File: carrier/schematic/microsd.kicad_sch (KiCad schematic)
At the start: 14 parts, among them J12001 TF-01A, U12001 TXS02612RTWR, U12002 TPD6E001RSER

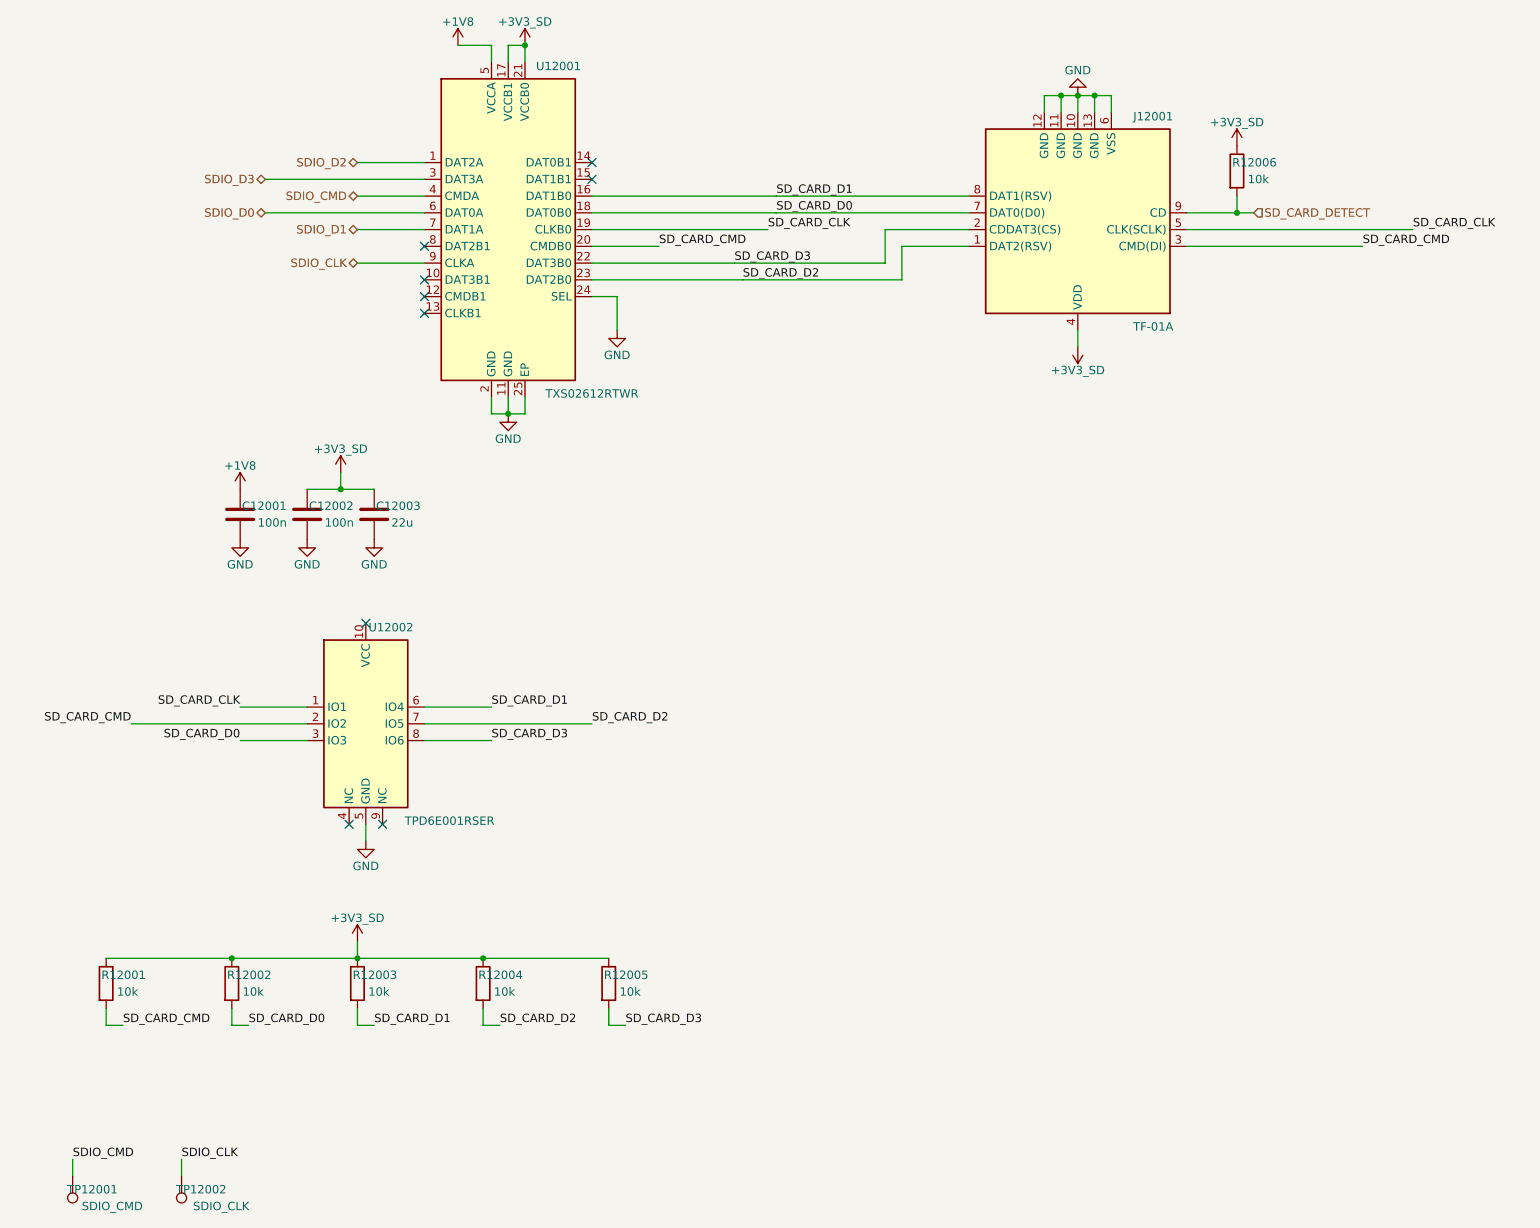
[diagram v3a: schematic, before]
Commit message: carrier: consolidated regen for round-6 audit fixes + PLAN RESOLVED
schgen board regen after SD-1 / HDMIRX-1 / HDMIRX-2 / LCD-1: 23 sheets, all
gates green (board-link, ERC=0, power-tree 16 regs/0 findings, testpoints,
SPICE 21 checks, visual). Goldens drift only on the 3 touched sheets
(microsd/hdmi_rx/lcd schematic+render), BOM (microsd:C4 100n, hdmi_rx:R5 10k,
lcd:C2 2.2u/C125847), reports, floorplan. PLAN findings marked RESOLVED
(HDMIRX-1 = documented verified-part DNP). selftest 44/44 + byte-deterministic.

Co-Authored-By: Claude Fable 5 <noreply@anthropic.com>
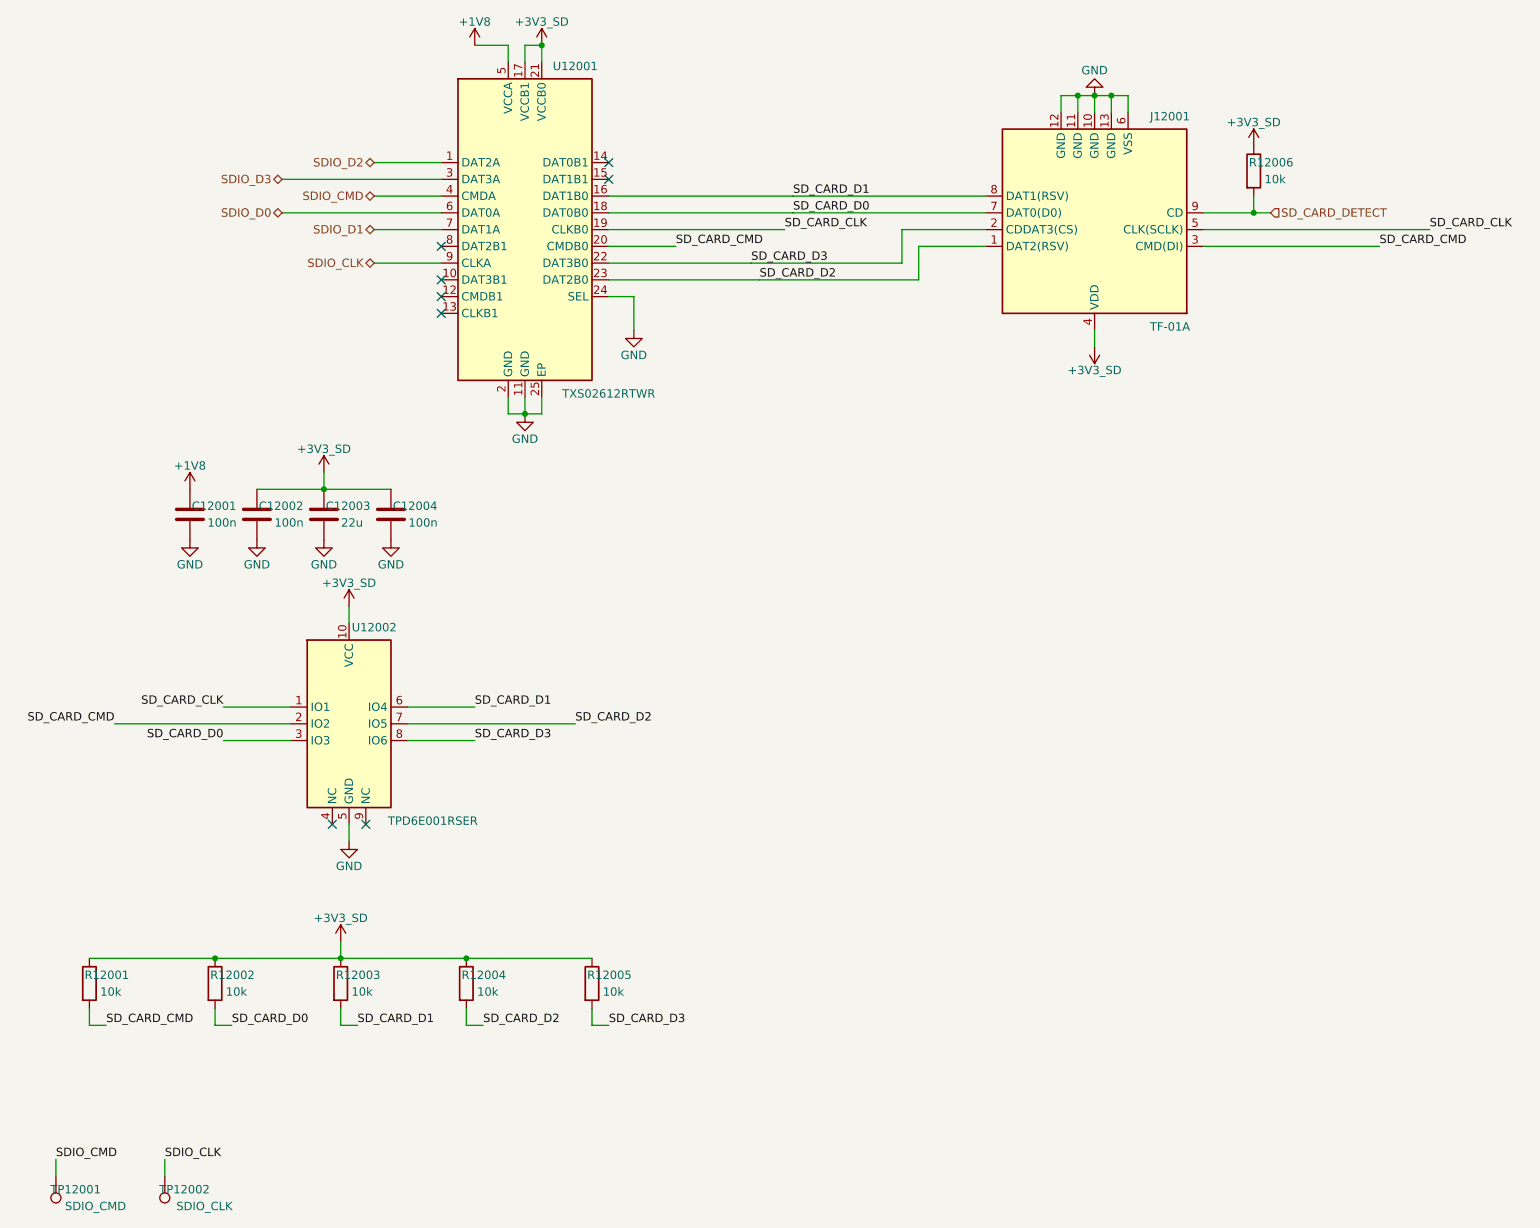
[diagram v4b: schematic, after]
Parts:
- added TP12002: SDIO_CLK, TestPoint:TestPoint_Pad_D1.5mm, symbol Connector:TestPoint
- C12004: renamed from U12002; value TPD6E001RSER -> 100n; footprint TPD6E001RSER:TPD6E001RSER -> (none); symbol TPD6E001RSER:TPD6E001RSER -> Device:C; LCSC C1973318 -> C14663
- R12005: renamed from TP12001; value SDIO_CMD -> 10k; footprint TestPoint:TestPoint_Pad_D1.5mm -> Resistor_SMD:R_0603_1608Metric; symbol Connector:TestPoint -> Device:R; BOM exclude -> (none); LCSC (none) -> C25804
- TP12001: renamed from TP12002; value SDIO_CLK -> SDIO_CMD
- U12002: renamed from R12001; value 10k -> TPD6E001RSER; footprint Resistor_SMD:R_0603_1608Metric -> TPD6E001RSER:TPD6E001RSER; symbol Device:R -> TPD6E001RSER:TPD6E001RSER; LCSC C25804 -> C1973318
- renumbered R12002 to R12001, R12003 to R12002, R12004 to R12003, R12005 to R12004
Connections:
- net +3V3_SD: now also C12004.1, R12005.1, U12002.10 (VCC); no longer U12002.1
- net GND: now also C12004.2, U12002.5 (GND); no longer C12004.5 (GND)
- net SDIO_CLK: now also TP12002.1; no longer TP12001.1
- net SDIO_CMD: now also TP12001.1; no longer R12005.1
- net SD_CARD_CLK: now also U12002.1 (IO1); no longer C12004.1 (IO1)
- net SD_CARD_CMD: now also R12001.2; no longer C12004.2 (IO2)
- net SD_CARD_D0: now also R12002.2, U12002.3 (IO3); no longer C12004.3 (IO3), R12001.2
- net SD_CARD_D1: now also R12003.2, U12002.6 (IO4); no longer C12004.6 (IO4), R12002.2
- net SD_CARD_D2: now also R12004.2, U12002.7 (IO5); no longer C12004.7 (IO5), R12003.2
- net SD_CARD_D3: now also R12005.2, U12002.8 (IO6); no longer C12004.8 (IO6), R12004.2
- no-connect marks 9 -> 8
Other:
- moved on the sheet: C12001, C12002, C12003, J12001, R12001, R12002, R12003, R12004, R12006, TP12001, U12001

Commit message: DEF-3: default footprints for inline passives + BOM footprint gate
16 inline Device:C/Device:R passives (decouple()/part() calls in microsd,
uart_bridge, usb_pd, usbc_otg) carried footprint='' — so the JLC BOM had 6
line items an assembler literally cannot place. model.part() now defaults a
standard SMD footprint when none is given: Device:R -> 0603, Device:C -> 0603
(or 0805 for >= 1 uF bulk), matching every inline passive's JLC Basic package
(100n/200p 0603, 10u/22u 0805, 1k/22k1/47k5 0603). use_part is unaffected (it
always supplies the library footprint). A new BOM FOOTPRINT GATE in cmd_board
fails the board if any BOM line is still footprint-less, backstopping the
non-passive case. board PASS, all 81 BOM lines placeable, 25 goldens match
(footprint is a hidden field — renders unchanged), selftest 44/44, m1 PASS.
The floorplan now gives those passives real courtyards.

Co-Authored-By: Claude Opus 4.8 <noreply@anthropic.com>
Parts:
- C12001, C12004: footprint (none) -> Capacitor_SMD:C_0603_1608Metric
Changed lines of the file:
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@@
 		(property
 			"Footprint"
-			""
+			"Capacitor_SMD:C_0603_1608Metric"
 			(at 123.19 133.35 0)
 			(effects
@@
 		(property
 			"Footprint"
-			""
+			"Capacitor_SMD:C_0603_1608Metric"
 			(at 153.67 133.35 0)
 			(effects

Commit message: DEF-6: netlist the HDMI-RX TMDS sink termination (new hdmi_rx_term sheet)
The HDMI-RX sink REQUIRES 8x 49.9 ohm/pair-to-AVCC source termination (a
7-series HR bank does not self-terminate TMDS_33) — without it HDMI RX simply
does not work. It had been carried for rounds as a docstring-only MANDATORY
layout note because the resistors belong at the FPGA-bank (receiver) end and
the connector-sheet placer could not anchor an off-sheet AVCC trunk. DEF-6
promotes it to a real, netlisted, gate-checked, BOM-counted network on its own
sheet hdmi_rx_term.py: 8x 49.9R (C114625) from HDMI_RX_{D2,D1,D0,CLK}_{P,N} to
AVCC = +3V3 (bank-33 VCCO IS +3V3, the correct TMDS_33 termination voltage).

LINK PASS (the 3-way TMDS merge with hdmi_rx + som_j2), powertree accepts the
~64 mA termination load, render clean (LAW 1), board PASS 26 sheets,
deterministic, selftest 44/44, m1 PASS.

The 100n/1u AVCC bypass is a documented layout note (not netlisted): the
placer has no pattern for a rail-to-rail cap with no host part on an IC-less
sheet (a tracked placer-robustness follow-up). Inserting the sheet
alphabetically re-stamps the per-sheet reference uniquification of the 15
downstream sheets (U11001->U12001 etc.) — deterministic, a known consequence
of the position-based hierarchy numbering.

Co-Authored-By: Claude Opus 4.8 <noreply@anthropic.com>
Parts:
- renumbered C12001 to C13001, C12002 to C13002, C12003 to C13003, C12004 to C13004, J12001 to J13001, R12001 to R13001, R12002 to R13002, R12003 to R13003, R12004 to R13004, R12005 to R13005, R12006 to R13006, TP12001 to TP13001, TP12002 to TP13002, U12001 to U13001, U12002 to U13002
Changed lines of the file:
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@@
 		(property
 			"Reference"
-			"U12001"
+			"U13001"
 			(at 181.61 65.405 0)
 			(effects
@@
 				(path
 					"/c2797150-7a6e-556a-82f5-fdda13c31368/d897b633-e4e1-5c36-ba27-9e08872325fa"
-					(reference "U12001")
+					(reference "U13001")
 					(unit 1)
 				)
@@
 		(property
 			"Reference"
-			"J12001"
+			"J13001"
 			(at 271.78 73.025 0)
 			(effects
@@
 				(path
 					"/c2797150-7a6e-556a-82f5-fdda13c31368/d897b633-e4e1-5c36-ba27-9e08872325fa"
-					(reference "J12001")
+					(reference "J13001")
 					(unit 1)
 				)
@@
 		(property
 			"Reference"
-			"R12006"
+			"R13006"
 			(at 287.123 80.01 0)
 			(effects
@@
 				(path
 					"/c2797150-7a6e-556a-82f5-fdda13c31368/d897b633-e4e1-5c36-ba27-9e08872325fa"
-					(reference "R12006")
+					(reference "R13006")
 					(unit 1)
 				)
@@
 		(property
 			"Reference"
-			"C12001"
+			"C13001"
 			(at 126.849 132.08 0)
 			(effects
@@
 				(path
 					"/c2797150-7a6e-556a-82f5-fdda13c31368/d897b633-e4e1-5c36-ba27-9e08872325fa"
-					(reference "C12001")
+					(reference "C13001")
 					(unit 1)
 				)
@@
 		(property
 			"Reference"
-			"C12002"
+			"C13002"
 			(at 137.009 132.08 0)
 			(effects
@@
 				(path
 					"/c2797150-7a6e-556a-82f5-fdda13c31368/d897b633-e4e1-5c36-ba27-9e08872325fa"
-					(reference "C12002")
+					(reference "C13002")
 					(unit 1)
 				)
@@
 		(property
 			"Reference"
-			"C12003"
+			"C13003"
 			(at 147.169 132.08 0)
 			(effects
@@
 				(path
 					"/c2797150-7a6e-556a-82f5-fdda13c31368/d897b633-e4e1-5c36-ba27-9e08872325fa"
-					(reference "C12003")
+					(reference "C13003")
 					(unit 1)
 				)
@@
 		(property
 			"Reference"
-			"C12004"
+			"C13004"
 			(at 157.329 132.08 0)
 			(effects
@@
 				(path
 					"/c2797150-7a6e-556a-82f5-fdda13c31368/d897b633-e4e1-5c36-ba27-9e08872325fa"
-					(reference "C12004")
+					(reference "C13004")
 					(unit 1)
 				)
@@
 		(property
 			"Reference"
-			"U12002"
+			"U13002"
 			(at 151.13 150.495 0)
 			(effects
@@
 				(path
 					"/c2797150-7a6e-556a-82f5-fdda13c31368/d897b633-e4e1-5c36-ba27-9e08872325fa"
-					(reference "U12002")
+					(reference "U13002")
 					(unit 1)
 				)
@@
 		(property
 			"Reference"
-			"R12001"
+			"R13001"
 			(at 110.593 203.2 0)
 			(effects
@@
 				(path
 					"/c2797150-7a6e-556a-82f5-fdda13c31368/d897b633-e4e1-5c36-ba27-9e08872325fa"
-					(reference "R12001")
+					(reference "R13001")
 					(unit 1)
 				)
@@
 		(property
 			"Reference"
-			"R12002"
+			"R13002"
 			(at 129.643 203.2 0)
 			(effects
@@
 				(path
 					"/c2797150-7a6e-556a-82f5-fdda13c31368/d897b633-e4e1-5c36-ba27-9e08872325fa"
-					(reference "R12002")
+					(reference "R13002")
 					(unit 1)
 				)
@@
 		(property
 			"Reference"
-			"R12003"
+			"R13003"
 			(at 148.693 203.2 0)
 			(effects
@@
 				(path
 					"/c2797150-7a6e-556a-82f5-fdda13c31368/d897b633-e4e1-5c36-ba27-9e08872325fa"
-					(reference "R12003")
+					(reference "R13003")
 					(unit 1)
 				)
@@
 		(property
 			"Reference"
-			"R12004"
+			"R13004"
 			(at 167.743 203.2 0)
 			(effects
@@
 				(path
 					"/c2797150-7a6e-556a-82f5-fdda13c31368/d897b633-e4e1-5c36-ba27-9e08872325fa"
-					(reference "R12004")
+					(reference "R13004")
 					(unit 1)
 				)
@@
 		(property
 			"Reference"
-			"R12005"
+			"R13005"
 			(at 186.792 203.2 0)
 			(effects
@@
 				(path
 					"/c2797150-7a6e-556a-82f5-fdda13c31368/d897b633-e4e1-5c36-ba27-9e08872325fa"
-					(reference "R12005")
+					(reference "R13005")
 					(unit 1)
 				)
@@
 		(property
 			"Reference"
-			"TP12001"
+			"TP13001"
 			(at 105.862 235.712 0)
 			(effects
@@
 				(path
 					"/c2797150-7a6e-556a-82f5-fdda13c31368/d897b633-e4e1-5c36-ba27-9e08872325fa"
-					(reference "TP12001")
+					(reference "TP13001")
 					(unit 1)
 				)
@@
 		(property
 			"Reference"
-			"TP12002"
+			"TP13002"
 			(at 122.372 235.712 0)
 			(effects
@@
 				(path
 					"/c2797150-7a6e-556a-82f5-fdda13c31368/d897b633-e4e1-5c36-ba27-9e08872325fa"
-					(reference "TP12002")
+					(reference "TP13002")
 					(unit 1)
 				)
@@
 		(property
 			"Reference"
-			"#PWR12001"
+			"#PWR13001"
 			(at 190.5 102.87 0)
 			(effects
@@
 				(path
 					"/c2797150-7a6e-556a-82f5-fdda13c31368/d897b633-e4e1-5c36-ba27-9e08872325fa"
-					(reference "#PWR12001")
+					(reference "#PWR13001")
 					(unit 1)
 				)
@@
 		(property
 			"Reference"
-			"#PWR12002"
+			"#PWR13002"
 			(at 176.53 59.69 0)
 			(effects
@@
 				(path
 					"/c2797150-7a6e-556a-82f5-fdda13c31368/d897b633-e4e1-5c36-ba27-9e08872325fa"
-					(reference "#PWR12002")
+					(reference "#PWR13002")
 					(unit 1)
 				)
@@
 		(property
 			"Reference"
-			"#PWR12003"
+			"#PWR13003"
 			(at 166.37 59.69 0)
 			(effects
@@
 				(path
 					"/c2797150-7a6e-556a-82f5-fdda13c31368/d897b633-e4e1-5c36-ba27-9e08872325fa"
-					(reference "#PWR12003")
+					(reference "#PWR13003")
 					(unit 1)
 				)
@@
 		(property
 			"Reference"
-			"#PWR12004"
+			"#PWR13004"
 			(at 173.99 115.57 0)
 			(effects
@@
 				(path
 					"/c2797150-7a6e-556a-82f5-fdda13c31368/d897b633-e4e1-5c36-ba27-9e08872325fa"
-					(reference "#PWR12004")
+					(reference "#PWR13004")
 					(unit 1)
 				)
@@
 		(property
 			"Reference"
-			"#PWR12005"
+			"#PWR13005"
 			(at 284.48 74.93 0)
 			(effects
@@
 				(path
 					"/c2797150-7a6e-556a-82f5-fdda13c31368/d897b633-e4e1-5c36-ba27-9e08872325fa"
-					(reference "#PWR12005")
+					(reference "#PWR13005")
 					(unit 1)
 				)
@@
 		(property
 			"Reference"
-			"#PWR12006"
+			"#PWR13006"
 			(at 260.35 67.31 0)
 			(effects
@@
 				(path
 					"/c2797150-7a6e-556a-82f5-fdda13c31368/d897b633-e4e1-5c36-ba27-9e08872325fa"
-					(reference "#PWR12006")
+					(reference "#PWR13006")
 					(unit 1)
 				)
@@
 		(property
 			"Reference"
-			"#PWR12007"
+			"#PWR13007"
 			(at 260.35 105.41 0)
 			(effects
@@
 				(path
 					"/c2797150-7a6e-556a-82f5-fdda13c31368/d897b633-e4e1-5c36-ba27-9e08872325fa"
-					(reference "#PWR12007")
+					(reference "#PWR13007")
 					(unit 1)
 				)
@@
 		(property
 			"Reference"
-			"#PWR12008"
+			"#PWR13008"
 			(at 123.19 134.62 0)
 			(effects
@@
 				(path
 					"/c2797150-7a6e-556a-82f5-fdda13c31368/d897b633-e4e1-5c36-ba27-9e08872325fa"
-					(reference "#PWR12008")
+					(reference "#PWR13008")
 					(unit 1)
 				)
@@
 		(property
 			"Reference"
-			"#PWR12009"
+			"#PWR13009"
 			(at 123.19 127 0)
 			(effects
@@
 				(path
 					"/c2797150-7a6e-556a-82f5-fdda13c31368/d897b633-e4e1-5c36-ba27-9e08872325fa"
-					(reference "#PWR12009")
+					(reference "#PWR13009")
 					(unit 1)
 				)
@@
 		(property
 			"Reference"
-			"#PWR12010"
+			"#PWR13010"
 			(at 133.35 134.62 0)
 			(effects
@@
 				(path
 					"/c2797150-7a6e-556a-82f5-fdda13c31368/d897b633-e4e1-5c36-ba27-9e08872325fa"
-					(reference "#PWR12010")
+					(reference "#PWR13010")
 					(unit 1)
 				)
@@
 		(property
 			"Reference"
-			"#PWR12011"
+			"#PWR13011"
 			(at 143.51 134.62 0)
 			(effects
@@
 				(path
 					"/c2797150-7a6e-556a-82f5-fdda13c31368/d897b633-e4e1-5c36-ba27-9e08872325fa"
-					(reference "#PWR12011")
+					(reference "#PWR13011")
 					(unit 1)
 				)
@@
 		(property
 			"Reference"
-			"#PWR12012"
+			"#PWR13012"
 			(at 153.67 134.62 0)
 			(effects
@@
 				(path
 					"/c2797150-7a6e-556a-82f5-fdda13c31368/d897b633-e4e1-5c36-ba27-9e08872325fa"
-					(reference "#PWR12012")
+					(reference "#PWR13012")
 					(unit 1)
 				)
@@
 		(property
 			"Reference"
-			"#PWR12013"
+			"#PWR13013"
 			(at 143.51 124.46 0)
 			(effects
@@
 				(path
 					"/c2797150-7a6e-556a-82f5-fdda13c31368/d897b633-e4e1-5c36-ba27-9e08872325fa"
-					(reference "#PWR12013")
+					(reference "#PWR13013")
 					(unit 1)
 				)
@@
 		(property
 			"Reference"
-			"#PWR12014"
+			"#PWR13014"
 			(at 147.32 144.78 0)
 			(effects
@@
 				(path
 					"/c2797150-7a6e-556a-82f5-fdda13c31368/d897b633-e4e1-5c36-ba27-9e08872325fa"
-					(reference "#PWR12014")
+					(reference "#PWR13014")
 					(unit 1)
 				)
@@
 		(property
 			"Reference"
-			"#PWR12015"
+			"#PWR13015"
 			(at 147.32 180.34 0)
 			(effects
@@
 				(path
 					"/c2797150-7a6e-556a-82f5-fdda13c31368/d897b633-e4e1-5c36-ba27-9e08872325fa"
-					(reference "#PWR12015")
+					(reference "#PWR13015")
 					(unit 1)
 				)
@@
 		(property
 			"Reference"
-			"#PWR12016"
+			"#PWR13016"
 			(at 146.05 195.58 0)
 			(effects
@@
 				(path
 					"/c2797150-7a6e-556a-82f5-fdda13c31368/d897b633-e4e1-5c36-ba27-9e08872325fa"
-					(reference "#PWR12016")
-					(unit 1)
-				)
+					(reference "#PWR13016")
+					(unit 1)
+				)

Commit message: genpolish: TITLE-1 — populate the schematic title block on every sheet
Every sheet rendered a blank Title/Rev/Date — the clearest 'not a real
schematic' tell. emit() now writes a (title_block ...) after the paper node:
title = the sheet circuit's title, company "Zynq SoM Carrier", and a
"<sheet> — generated by schgen (do not hand-edit)" comment. NO date node — a
wall-clock date would break byte-determinism; the content-derived fields keep
every rebuild identical. Verified on A4 (usb_pd) and the dense A3 (power): the
block fills the standard reserved corner with zero drawing overlap. All 26
sheets, goldens re-blessed, board PASS + deterministic, selftest 53/53, m1,
pytest 147.

Co-Authored-By: Claude Opus 4.8 <noreply@anthropic.com>
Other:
- company: (none) -> Zynq SoM Carrier
- title: (none) -> microSD slot (1.8V SoM <-> 3.3V card, TXS02612)
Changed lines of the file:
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@@
 	(generator_version "1.0")
 	(paper "A3")
+	(title_block
+		(title "microSD slot (1.8V SoM <-> 3.3V card, TXS02612)")
+		(company "Zynq SoM Carrier")
+		(comment 1 "microsd — generated by schgen (do not hand-edit)")
+	)
 	(wire
 		(pts
